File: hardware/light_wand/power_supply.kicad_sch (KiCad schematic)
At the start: 13 parts, among them U1 TLV61070A

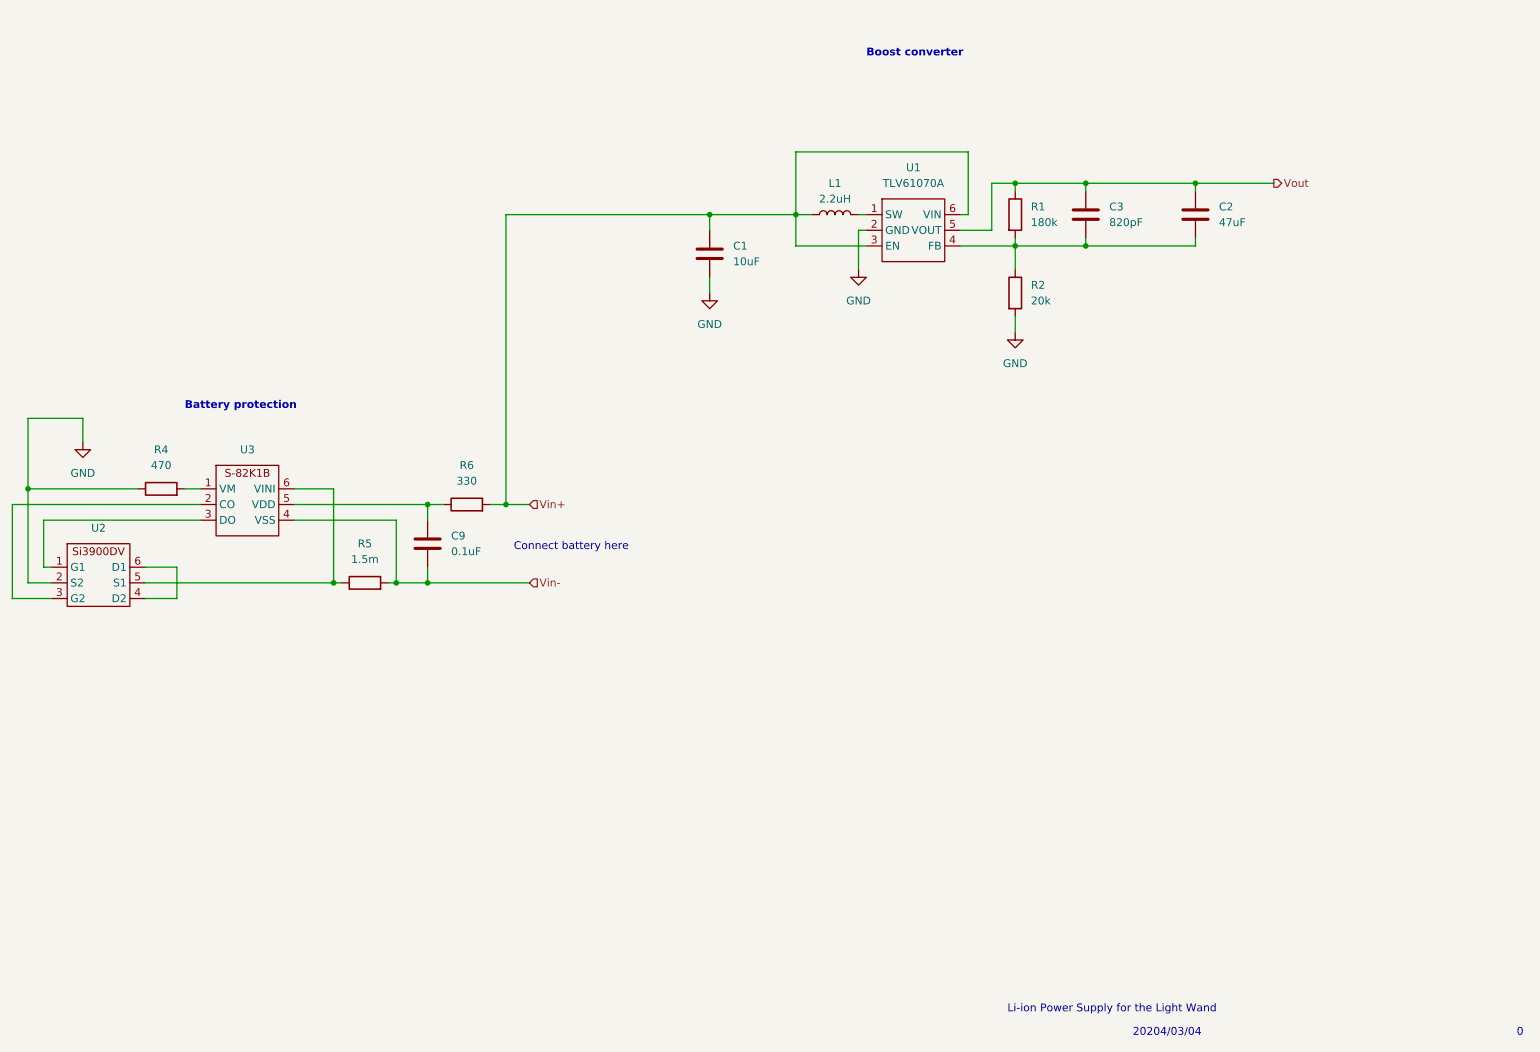
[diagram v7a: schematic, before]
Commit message: Added footprints to everything in the power supply
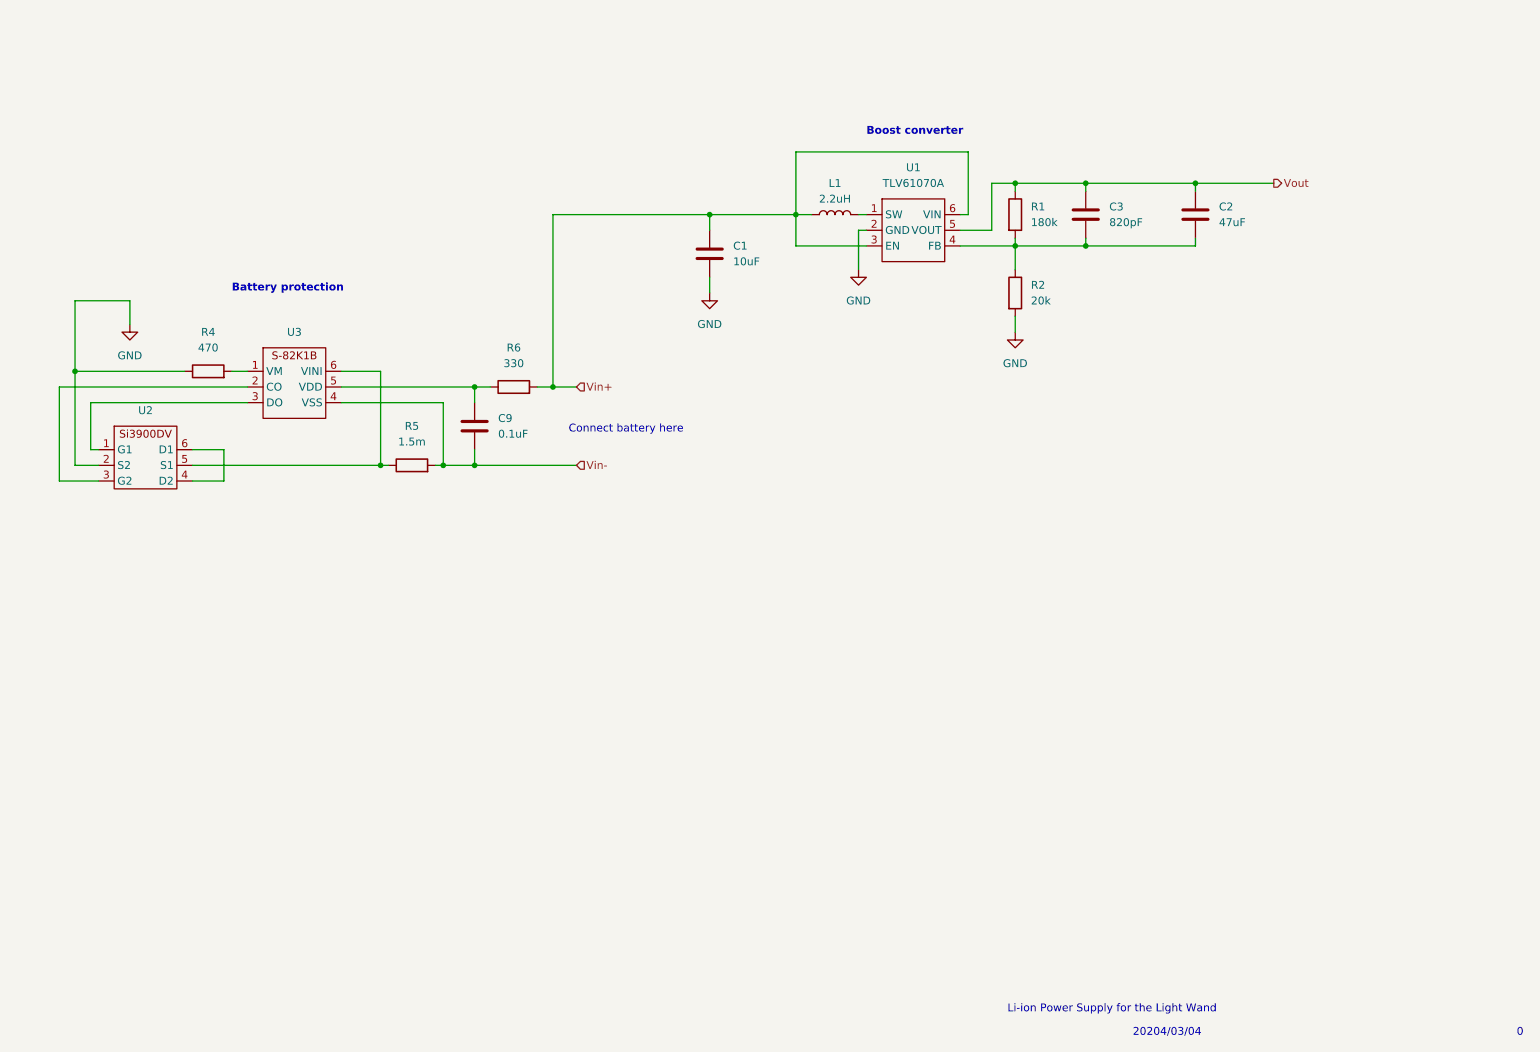
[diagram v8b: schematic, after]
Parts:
- C1, C2, C3, C9: footprint (none) -> Capacitor_SMD:C_0603_1608Metric
- R1, R2, R4, R6: footprint (none) -> Resistor_SMD:R_0201_0603Metric
- R5: footprint (none) -> Resistor_SMD:R_2512_6332Metric; Purchase Link (none) -> https://www.digikey.com/en/products/detail/riedon/CSRL3-0R0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
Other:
- moved on the sheet: C9, R4, R5, R6, U2, U3
